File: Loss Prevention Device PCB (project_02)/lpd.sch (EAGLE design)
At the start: 4 parts, among them U2 GT-U7, U3 HM-10

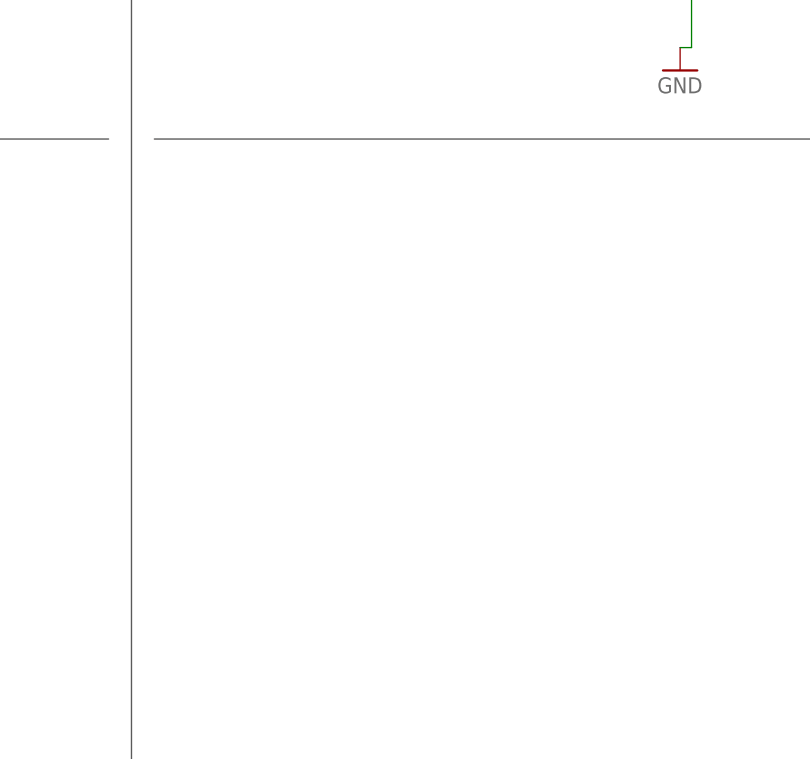
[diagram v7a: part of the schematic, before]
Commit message: Silkscreen cleanup
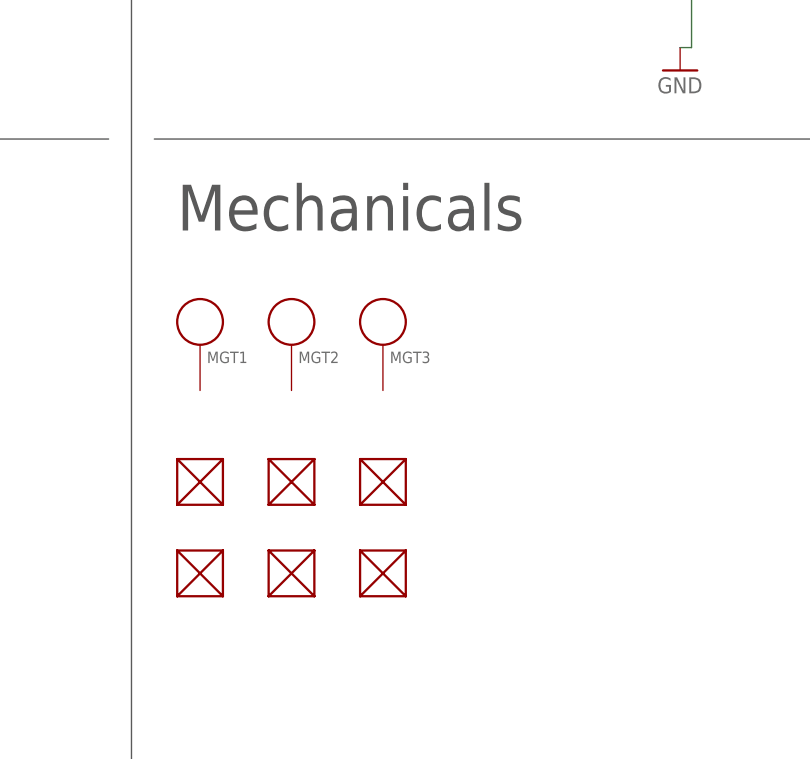
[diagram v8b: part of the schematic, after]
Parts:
- added FUD1, FUD2, FUD3, FUD4, FUD5, FUD6: FIDUCIAL, lpd:FIDUCIAL
- added MGT1, MGT2, MGT3: MOUNTING_HOLE, lpd:MOUNTING_HOLE
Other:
- note added: "Mechanicals"
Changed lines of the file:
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@@
 <part name="GND5" library="lpd" deviceset="GND" device=""/>
 <part name="GND6" library="lpd" deviceset="GND" device=""/>
+<part name="MGT1" library="lpd" deviceset="MOUNTING_HOLE" device=""/>
+<part name="MGT2" library="lpd" deviceset="MOUNTING_HOLE" device=""/>
+<part name="MGT3" library="lpd" deviceset="MOUNTING_HOLE" device=""/>
+<part name="FUD1" library="lpd" deviceset="FIDUCIAL" device=""/>
+<part name="FUD2" library="lpd" deviceset="FIDUCIAL" device=""/>
+<part name="FUD3" library="lpd" deviceset="FIDUCIAL" device=""/>
+<part name="FUD4" library="lpd" deviceset="FIDUCIAL" device=""/>
+<part name="FUD5" library="lpd" deviceset="FIDUCIAL" device=""/>
+<part name="FUD6" library="lpd" deviceset="FIDUCIAL" device=""/>
 </parts>
 <sheets>
@@
 <text x="266.7" y="243.84" size="5.08" layer="97" font="vector">Bluetooth Module</text>
 <wire x1="152.4" y1="142.24" x2="5.08" y2="142.24" width="0.1524" layer="97"/>
+<text x="261.62" y="132.08" size="5.08" layer="97" font="vector">Mechanicals</text>
 </plain>
 <instances>
@@
 <attribute name="VALUE" x="226.06" y="78.74" size="1.778" layer="96"/>
 </instance>
+<instance part="MGT1" gate="G$1" x="264.16" y="119.38" smashed="yes">
+<attribute name="NAME" x="264.922" y="117.348" size="1.27" layer="95"/>
+</instance>
+<instance part="MGT2" gate="G$1" x="274.32" y="119.38" smashed="yes">
+<attribute name="NAME" x="275.082" y="117.348" size="1.27" layer="95"/>
+</instance>
+<instance part="MGT3" gate="G$1" x="284.48" y="119.38" smashed="yes">
+<attribute name="NAME" x="285.242" y="117.348" size="1.27" layer="95"/>
+</instance>
+<instance part="FUD1" gate="G$1" x="264.16" y="104.14" smashed="yes"/>
+<instance part="FUD2" gate="G$1" x="274.32" y="104.14" smashed="yes"/>
+<instance part="FUD3" gate="G$1" x="284.48" y="104.14" smashed="yes"/>
+<instance part="FUD4" gate="G$1" x="264.16" y="93.98" smashed="yes"/>
+<instance part="FUD5" gate="G$1" x="274.32" y="93.98" smashed="yes"/>
+<instance part="FUD6" gate="G$1" x="284.48" y="93.98" smashed="yes"/>
 </instances>
 <busses>
